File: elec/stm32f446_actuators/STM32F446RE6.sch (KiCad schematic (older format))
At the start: 24 parts, among them J3 USART, J4 SWD, SW1 RESET, U3 MIC5504-3.3YM5, U4 STM32F446RETx, Y2 8MHz(16pF)[N/A]

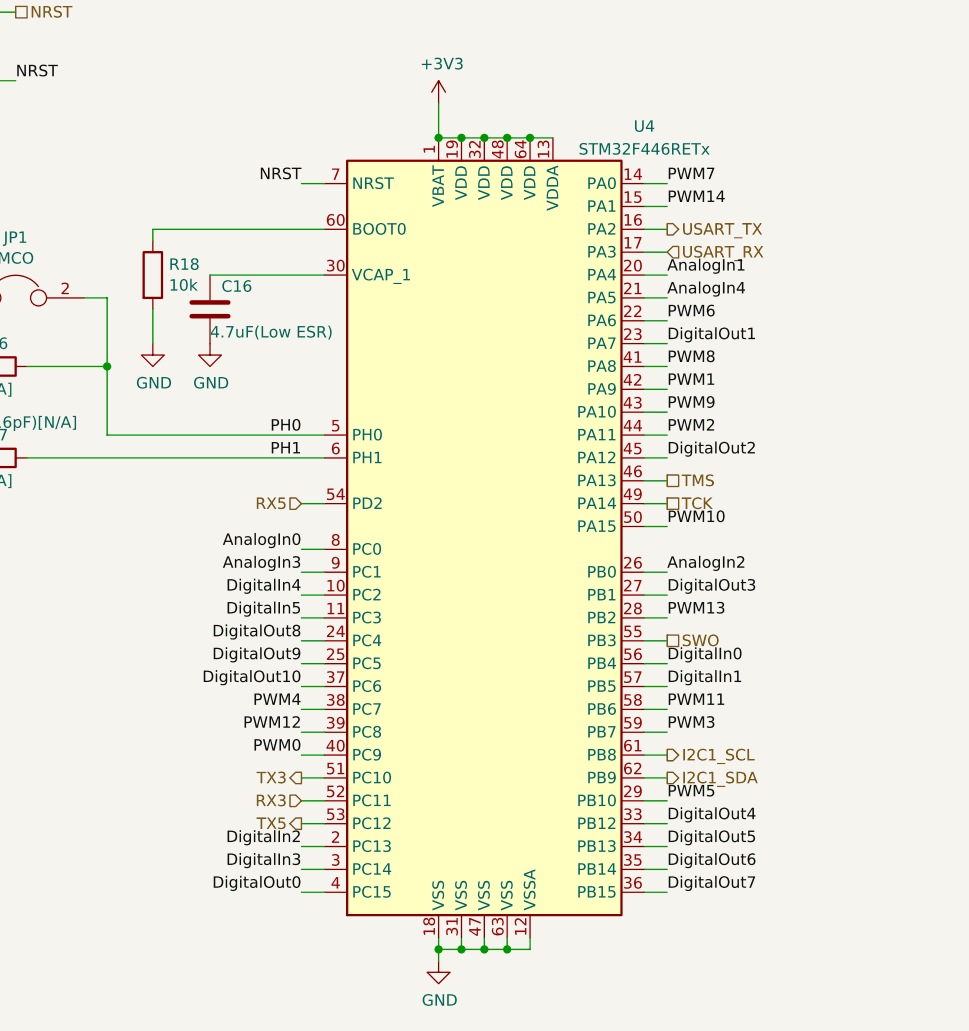
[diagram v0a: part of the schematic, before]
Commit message: Add routed PCB without GNDs and update µC sch
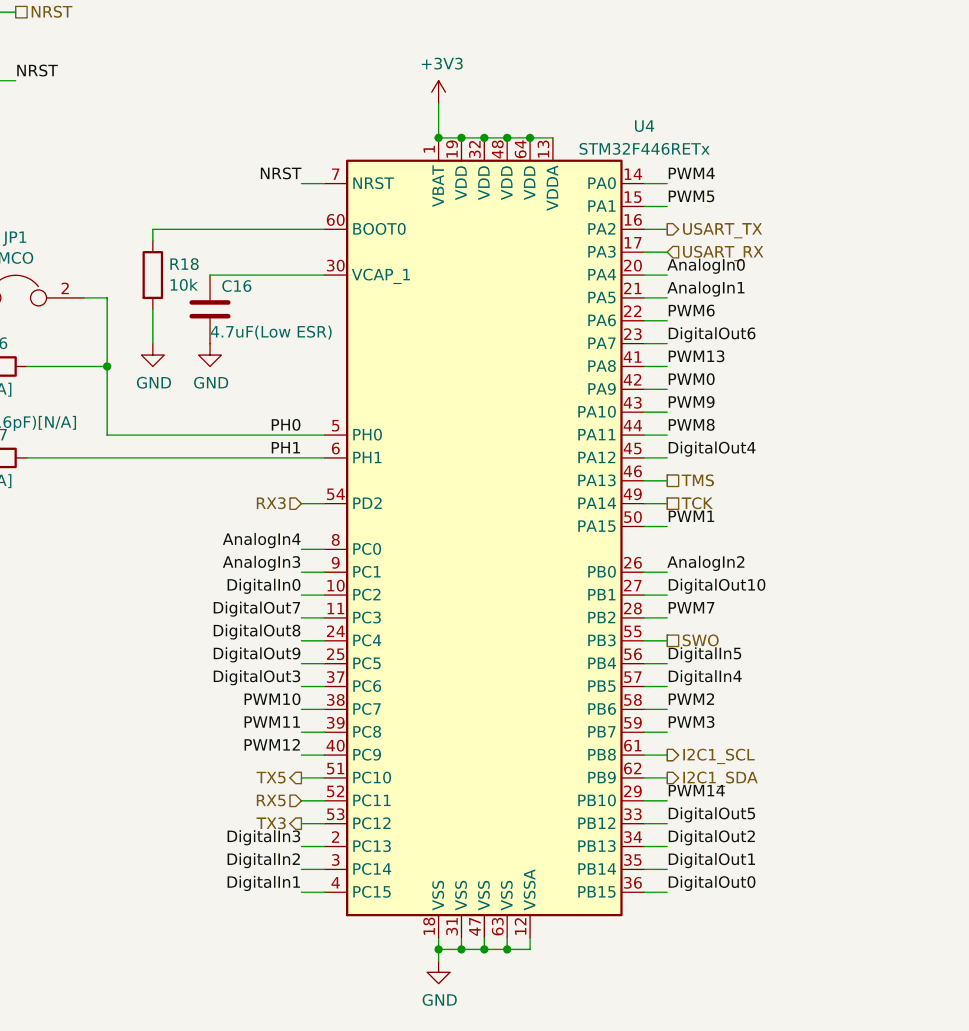
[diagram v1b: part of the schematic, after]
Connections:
- net AnalogIn0: now also U4.20 (PA4); no longer U4.8 (PC0)
- net AnalogIn1: now also U4.21 (PA5); no longer U4.20 (PA4)
- net AnalogIn4: now also U4.8 (PC0); no longer U4.21 (PA5)
- net DigitalIn0: now also U4.10 (PC2); no longer U4.56 (PB4)
- net DigitalIn1: now also U4.4 (PC15); no longer U4.57 (PB5)
- net DigitalIn2: now also U4.3 (PC14); no longer U4.2 (PC13)
- net DigitalIn3: now also U4.2 (PC13); no longer U4.3 (PC14)
- net DigitalIn4: now also U4.57 (PB5); no longer U4.10 (PC2)
- net DigitalIn5: now also U4.56 (PB4); no longer U4.11 (PC3)
- net DigitalOut0: now also U4.36 (PB15); no longer U4.4 (PC15)
- net DigitalOut1: now also U4.35 (PB14); no longer U4.23 (PA7)
- net DigitalOut10: now also U4.27 (PB1); no longer U4.37 (PC6)
- net DigitalOut2: now also U4.34 (PB13); no longer U4.45 (PA12)
- net DigitalOut3: now also U4.37 (PC6); no longer U4.27 (PB1)
- net DigitalOut4: now also U4.45 (PA12); no longer U4.33 (PB12)
- net DigitalOut5: now also U4.33 (PB12); no longer U4.34 (PB13)
- net DigitalOut6: now also U4.23 (PA7); no longer U4.35 (PB14)
- net DigitalOut7: now also U4.11 (PC3); no longer U4.36 (PB15)
- net PWM0: now also U4.42 (PA9); no longer U4.40 (PC9)
- net PWM1: now also U4.50 (PA15); no longer U4.42 (PA9)
- net PWM10: now also U4.38 (PC7); no longer U4.50 (PA15)
- net PWM11: now also U4.39 (PC8); no longer U4.58 (PB6)
- net PWM12: now also U4.40 (PC9); no longer U4.39 (PC8)
- net PWM13: now also U4.41 (PA8); no longer U4.28 (PB2)
- net PWM14: now also U4.29 (PB10); no longer U4.15 (PA1)
- net PWM2: now also U4.58 (PB6); no longer U4.44 (PA11)
- net PWM4: now also U4.14 (PA0); no longer U4.38 (PC7)
- net PWM5: now also U4.15 (PA1); no longer U4.29 (PB10)
- net PWM7: now also U4.28 (PB2); no longer U4.14 (PA0)
- net PWM8: now also U4.44 (PA11); no longer U4.41 (PA8)
- net RX3: now also U4.54 (PD2); no longer U4.52 (PC11)
- net RX5: now also U4.52 (PC11); no longer U4.54 (PD2)
- net TX3: now also U4.53 (PC12); no longer U4.51 (PC10)
- net TX5: now also U4.51 (PC10); no longer U4.53 (PC12)
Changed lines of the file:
@@
 EESchema Schematic File Version 4
-LIBS:stm32f446_actuators-cache
+LIBS:STM32F446RE6-cache
 EELAYER 30 0
 EELAYER END
 $Descr A4 11693 8268
 encoding utf-8
-Sheet 3 4
+Sheet 1 1
 Title ""
 Date ""
@@
 $EndComp
 $Comp
-L power:GND #PWR?
+L power:GND #PWR0101
 U 1 1 5E88322F
 P 8400 2250
-AR Path="/5E88322F" Ref="#PWR?"  Part="1"
+AR Path="/5E88322F" Ref="#PWR0101"  Part="1"
 AR Path="/5E88152D/5E88322F" Ref="#PWR040"  Part="1"
 F 0 "#PWR040" H 8400 2000 50  0001 C CNN
@@
 AR Path="/5E649856/5E85F280" Ref="#PWR?"  Part="1"
 AR Path="/5E88152D/5E85F280" Ref="#PWR035"  Part="1"
+AR Path="/5E85F280" Ref="#PWR035"  Part="1"
 F 0 "#PWR035" H 3100 1500 50  0001 C CNN
 F 1 "GND" H 3105 1577 50  0000 C CNN
@@
 AR Path="/5E649856/5E85F28E" Ref="R?"  Part="1"
 AR Path="/5E88152D/5E85F28E" Ref="R19"  Part="1"
+AR Path="/5E85F28E" Ref="R19"  Part="1"
 F 0 "R19" H 3170 1296 50  0000 L CNN
 F 1 "56" H 3170 1205 50  0000 L CNN
@@
 AR Path="/5E649856/5E85F294" Ref="D?"  Part="1"
 AR Path="/5E88152D/5E85F294" Ref="D5"  Part="1"
+AR Path="/5E85F294" Ref="D5"  Part="1"
 F 0 "D5" V 3139 1433 50  0000 R CNN
 F 1 "LED_R" V 3048 1433 50  0000 R CNN
@@
 AR Path="/5E649856/5E85F29B" Ref="C?"  Part="1"
 AR Path="/5E88152D/5E85F29B" Ref="C15"  Part="1"
+AR Path="/5E85F29B" Ref="C15"  Part="1"
 F 0 "C15" H 2665 1546 50  0000 L CNN
 F 1 "1uF" H 2665 1455 50  0000 L CNN
@@
 AR Path="/5E649856/5E85F2A1" Ref="C?"  Part="1"
 AR Path="/5E88152D/5E85F2A1" Ref="C11"  Part="1"
+AR Path="/5E85F2A1" Ref="C11"  Part="1"
 F 0 "C11" H 1465 1546 50  0000 L CNN
 F 1 "1uF" H 1465 1455 50  0000 L CNN
@@
 AR Path="/5E649856/5E85F2A7" Ref="#PWR?"  Part="1"
 AR Path="/5E88152D/5E85F2A7" Ref="#PWR032"  Part="1"
+AR Path="/5E85F2A7" Ref="#PWR032"  Part="1"
 F 0 "#PWR032" H 2550 1500 50  0001 C CNN
 F 1 "GND" H 2555 1577 50  0000 C CNN
@@
 AR Path="/5E649856/5E85F2AD" Ref="#PWR?"  Part="1"
 AR Path="/5E88152D/5E85F2AD" Ref="#PWR028"  Part="1"
+AR Path="/5E85F2AD" Ref="#PWR028"  Part="1"
 F 0 "#PWR028" H 1350 1500 50  0001 C CNN
 F 1 "GND" H 1355 1577 50  0000 C CNN
@@
 AR Path="/5E649856/5E85F2B3" Ref="#PWR?"  Part="1"
 AR Path="/5E88152D/5E85F2B3" Ref="#PWR030"  Part="1"
+AR Path="/5E85F2B3" Ref="#PWR030"  Part="1"
 F 0 "#PWR030" H 1950 1500 50  0001 C CNN
 F 1 "GND" H 1955 1577 50  0000 C CNN
@@
 AR Path="/5E649856/5E85F2BB" Ref="#PWR?"  Part="1"
 AR Path="/5E88152D/5E85F2BB" Ref="#PWR031"  Part="1"
+AR Path="/5E85F2BB" Ref="#PWR031"  Part="1"
 F 0 "#PWR031" H 2550 750 50  0001 C CNN
 F 1 "+3V3" H 2565 1073 50  0000 C CNN
@@
 AR Path="/5E649856/5E85F2C9" Ref="U?"  Part="1"
 AR Path="/5E88152D/5E85F2C9" Ref="U3"  Part="1"
+AR Path="/5E85F2C9" Ref="U3"  Part="1"
 F 0 "U3" H 1950 1517 50  0000 C CNN
 F 1 "MIC5504-3.3YM5" H 1950 1426 50  0000 C CNN
@@
 	5000 3350 4900 3350
 Text Label 3400 5850 2    50   ~ 0
+PWM12
+Text Label 5000 4250 0    50   ~ 0
 PWM0
-Text Label 5000 4250 0    50   ~ 0
-PWM1
 Text Label 5000 4450 0    50   ~ 0
-PWM2
+PWM8
 Text Label 5000 5750 0    50   ~ 0
 PWM3
 Text Label 3400 5650 2    50   ~ 0
-PWM4
+PWM10
 Text Label 5000 3950 0    50   ~ 0
 PWM6
 Text Label 5000 3350 0    50   ~ 0
-PWM7
+PWM4
 Text Label 5000 4150 0    50   ~ 0
-PWM8
+PWM13
 Text Label 5000 4350 0    50   ~ 0
 PWM9
 Text Label 5000 4850 0    50   ~ 0
-PWM10
+PWM1
 Text Label 5000 5650 0    50   ~ 0
-PWM11
+PWM2
 Wire Bus Line
 	7400 3550 7550 3550
-Text HLabel 3400 5950 0    50   Output ~ 0
-TX3
-Text HLabel 3400 6050 0    50   Input ~ 0
-RX3
 Wire Wire Line
 	3400 5950 3500 5950
@@
 	3400 6150 3500 6150
 Text Label 3400 5750 2    50   ~ 0
-PWM12
+PWM11
 Wire Wire Line
 	3400 5750 3500 5750
 Text Label 5000 5250 0    50   ~ 0
-PWM13
+PWM7
 Wire Wire Line
 	5000 5250 4900 5250
@@
 	4900 5950 5000 5950
 Text Label 3400 4950 2    50   ~ 0
+AnalogIn4
+Text Label 5000 3750 0    50   ~ 0
 AnalogIn0
-Text Label 5000 3750 0    50   ~ 0
-AnalogIn1
 Text Label 5000 5050 0    50   ~ 0
 AnalogIn2
@@
 	7400 3750 7550 3750
 Text Label 5000 3450 0    50   ~ 0
+PWM5
+Text Label 5000 6050 0    50   ~ 0
 PWM14
-Text HLabel 3400 4750 0    50   Input ~ 0
-RX5
-Text HLabel 3400 6150 0    50   Output ~ 0
-TX5
-Text Label 5000 6050 0    50   ~ 0
-PWM5
 Wire Wire Line
 	3400 4950 3500 4950
@@
 	7400 3950 7550 3950
 Text Label 5000 5150 0    50   ~ 0
-DigitalOut3
+DigitalOut10
 Text Label 5000 4550 0    50   ~ 0
-DigitalOut2
+DigitalOut4
 Text Label 5000 4050 0    50   ~ 0
-DigitalOut1
+DigitalOut6
 Text Label 5000 5550 0    50   ~ 0
-DigitalIn1
+DigitalIn4
 Text Label 5000 5450 0    50   ~ 0
+DigitalIn5
+Text Label 3400 6350 2    50   ~ 0
+DigitalIn2
+Text Label 3400 6250 2    50   ~ 0
+DigitalIn3
+Text Label 3400 5250 2    50   ~ 0
+DigitalOut7
+Text Label 3400 5150 2    50   ~ 0
 DigitalIn0
-Text Label 3400 6350 2    50   ~ 0
-DigitalIn3
-Text Label 3400 6250 2    50   ~ 0
-DigitalIn2
-Text Label 3400 5250 2    50   ~ 0
-DigitalIn5
-Text Label 3400 5150 2    50   ~ 0
-DigitalIn4
 Wire Wire Line
 	5000 4050 4900 4050
@@
 	5000 6150 4900 6150
 Text Label 5000 6150 0    50   ~ 0
-DigitalOut4
+DigitalOut5
 Text Label 5000 6250 0    50   ~ 0
-DigitalOut5
+DigitalOut2
 Text Label 5000 6350 0    50   ~ 0
-DigitalOut6
+DigitalOut1
 Text Label 5000 6450 0    50   ~ 0
-DigitalOut7
+DigitalOut0
 Text Label 3400 5350 2    50   ~ 0
 DigitalOut8
@@
 DigitalOut9
 Text Label 3400 5550 2    50   ~ 0
-DigitalOut10
+DigitalOut3
 Text Label 5000 3850 0    50   ~ 0
-AnalogIn4
+AnalogIn1
 Text Label 3400 6450 2    50   ~ 0
-DigitalOut0
+DigitalIn1
+Text HLabel 3400 4750 0    50   Input ~ 0
+RX3
+Text HLabel 3400 6050 0    50   Input ~ 0
+RX5
+Text HLabel 3400 6150 0    50   Output ~ 0
+TX3
+Text HLabel 3400 5950 0    50   Output ~ 0
+TX5
 $EndSCHEMATC

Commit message: GND done, silkscreen done and some minor fixes
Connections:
- net +5V renamed +5V_STM
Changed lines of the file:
@@
 EESchema Schematic File Version 4
-LIBS:STM32F446RE6-cache
+LIBS:stm32f446_actuators-cache
 EELAYER 30 0
 EELAYER END
 $Descr A4 11693 8268
 encoding utf-8
-Sheet 1 1
+Sheet 3 4
 Title ""
 Date ""
@@
 $EndComp
 Text HLabel 1050 1050 0    50   Input ~ 0
-+5V
++5V_STM
 Wire Wire Line
 	1350 1750 1350 1650
@@
 Wire Wire Line
 	1350 1050 1550 1050
-Wire Wire Line
-	1350 900  1350 1050
 $Comp
 L Regulator_Linear:MIC5504-3.3YM5 U?
@@
 F 3 "http://ww1.microchip.com/downloads/en/DeviceDoc/MIC550X.pdf" H 1700 1400 50  0001 C CNN
 	1    1950 1150
-	1    0    0    -1
-$EndComp
-$Comp
-L power:+5V #PWR027
-U 1 1 5E860708
-P 1350 900
-F 0 "#PWR027" H 1350 750 50  0001 C CNN
-F 1 "+5V" H 1365 1073 50  0000 C CNN
-F 2 "" H 1350 900 50  0001 C CNN
-F 3 "" H 1350 900 50  0001 C CNN
-	1    1350 900
 	1    0    0    -1
 $EndComp
@@
 Text HLabel 3400 5950 0    50   Output ~ 0
 TX5
+Text Label 1350 800  0    50   ~ 0
++5V_STM
+Wire Wire Line
+	1350 800  1350 1050
 $EndSCHEMATC

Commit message: Fix serial 3 and 5 reversed labels
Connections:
- net RX3: now also U4.52 (PC11); no longer U4.54 (PD2)
- net RX5: now also U4.54 (PD2); no longer U4.52 (PC11)
- net TX3: now also U4.51 (PC10); no longer U4.53 (PC12)
- net TX5: now also U4.53 (PC12); no longer U4.51 (PC10)
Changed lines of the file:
@@
 DigitalIn1
 Text HLabel 3400 4750 0    50   Input ~ 0
+RX5
+Text HLabel 3400 6050 0    50   Input ~ 0
 RX3
-Text HLabel 3400 6050 0    50   Input ~ 0
-RX5
 Text HLabel 3400 6150 0    50   Output ~ 0
+TX5
+Text HLabel 3400 5950 0    50   Output ~ 0
 TX3
-Text HLabel 3400 5950 0    50   Output ~ 0
-TX5
 Text Label 1350 800  0    50   ~ 0
 +5V_STM
